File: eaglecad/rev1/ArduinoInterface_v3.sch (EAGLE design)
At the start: 49 parts, among them IC1 74LS00N, IC10 74LS241N, IC11 74LS20N, IC3 74LS30N, IC5 74S74N, IC6 74LS139N, IC7 74LS155N, IC8 74LS241N, IC9 7805TV, J1 Connector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

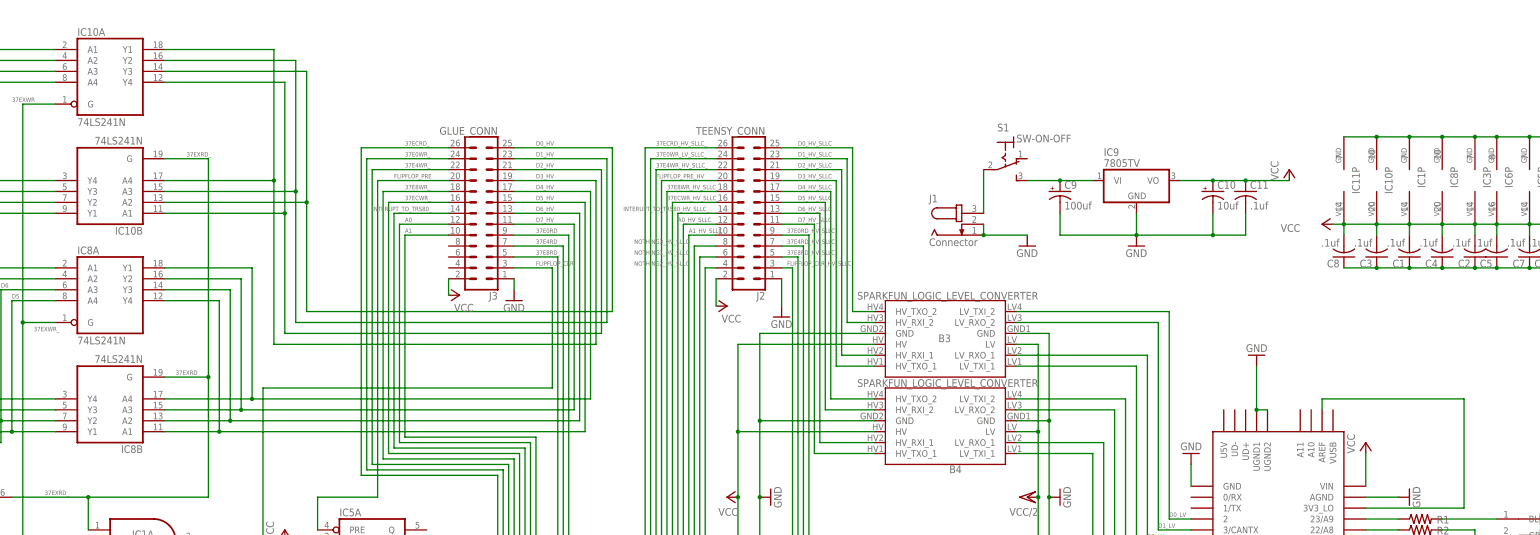
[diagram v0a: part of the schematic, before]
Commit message: updated schematic to fix 74LS241/74LS244 mixup
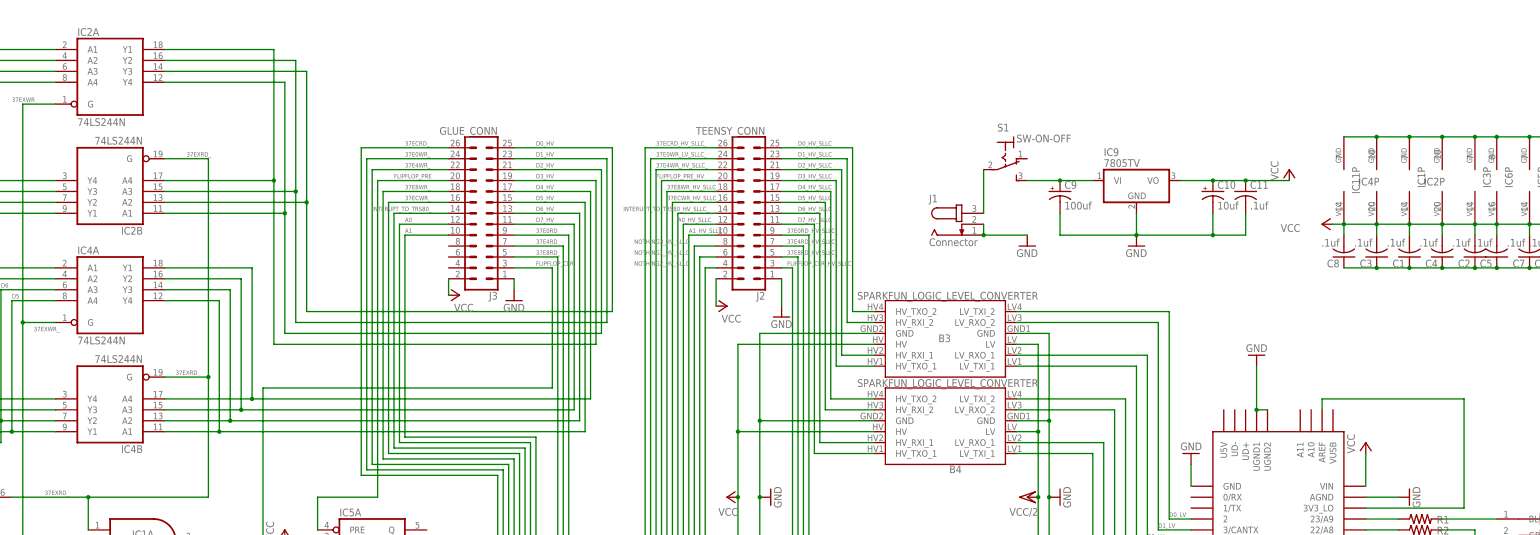
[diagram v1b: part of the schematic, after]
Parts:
- removed IC10, IC8: 74LS241N, 74xx-us:74LS241N
- added IC2, IC4: 74LS244N, 74xx-us:74LS244N
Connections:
- net 37EXRD_: now also IC2B.G, IC4B.G; no longer IC10B.G, IC8B.G
- net 37EXWR_: now also IC2A.G, IC4A.G; no longer IC10A.G, IC8A.G
- net D0: now also IC2A.A3, IC2B.Y2; no longer IC10A.A3, IC10B.Y2
- net D0_HV: now also IC2A.Y3, IC2B.A2; no longer IC10A.Y3, IC10B.A2
- net D1: now also IC2A.A2, IC2B.Y3; no longer IC10A.A2, IC10B.Y3
- net D1_HV: now also IC2A.Y2, IC2B.A3; no longer IC10A.Y2, IC10B.A3
- net D2: now also IC2A.A4, IC2B.Y1; no longer IC10A.A4, IC10B.Y1
- net D2_HV: now also IC2A.Y4, IC2B.A1; no longer IC10A.Y4, IC10B.A1
- net D3: now also IC2A.A1, IC2B.Y4; no longer IC10A.A1, IC10B.Y4
- net D3_HV: now also IC2A.Y1, IC2B.A4; no longer IC10A.Y1, IC10B.A4
- net D4: now also IC4A.A1, IC4B.Y4; no longer IC8A.A1, IC8B.Y4
- net D4_HV: now also IC4A.Y1, IC4B.A4; no longer IC8A.Y1, IC8B.A4
- net D5: now also IC4A.A4, IC4B.Y1; no longer IC8A.A4, IC8B.Y1
- net D5_HV: now also IC4A.Y4, IC4B.A1; no longer IC8A.Y4, IC8B.A1
- net D6: now also IC4A.A3, IC4B.Y2; no longer IC8A.A3, IC8B.Y2
- net D6_HV: now also IC4A.Y3, IC4B.A2; no longer IC8A.Y3, IC8B.A2
- net D7: now also IC4A.A2, IC4B.Y3; no longer IC8A.A2, IC8B.Y3
- net D7_HV: now also IC4A.Y2, IC4B.A3; no longer IC8A.Y2, IC8B.A3
- net GND: now also IC2P.GND, IC4P.GND; no longer IC10P.GND, IC8P.GND
- net VCC: now also IC2P.VCC, IC4P.VCC; no longer IC10P.VCC, IC8P.VCC
